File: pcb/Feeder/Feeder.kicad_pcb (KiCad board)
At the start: 2 copper layers, 19.8 x 10.8 mm, 4 parts, among them J1 Controller, J2 N20, J3 Servo/Feedback

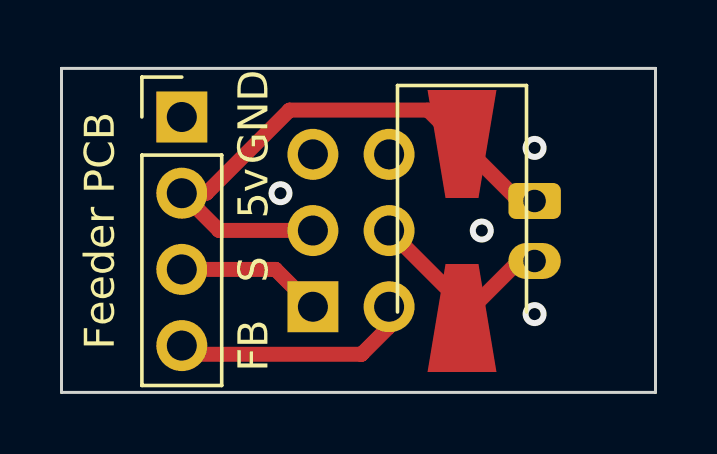
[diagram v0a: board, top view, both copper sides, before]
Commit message: re-panelized to use silk screen between small PCBs to reduce cost
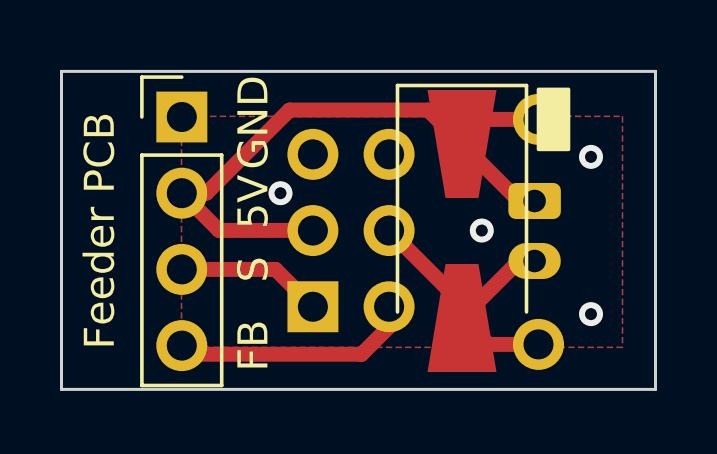
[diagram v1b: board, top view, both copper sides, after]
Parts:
- added D2: 1N4001, CustomDiode:D_SMA-SMB_Universal_Handsoldering_Holes, F.Cu at (154.0, 94.2)
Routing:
- net /N20-GND: track 7.13 -> 10.0 mm
- net +5V: track 19.0 -> 21.9 mm
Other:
- board size 19.8 x 10.8 mm -> 19.8 x 10.6 mm
- board text added: "+"
- board text added: "5V"
- board text removed: "+++"
- board text removed: "5v"
- board text removed: "JLCJLCJLCJLC"
